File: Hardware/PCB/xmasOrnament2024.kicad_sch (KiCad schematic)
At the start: 54 parts, among them IC1 TP4056-42, Q1 AO3401A, Q2 CJ3400, SW1 BZCN_TSA007A1518B03, SW2 BZCN_TSA007A1518B03, U1 STM32C011F6

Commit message: Fixes.
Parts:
- added R14: 100k, Borna KiCAD Library:R0603, symbol Borna KiCAD Libary:R0603
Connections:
- net GND: now also R14.2
- net SW_CLK: now also R14.1
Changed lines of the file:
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@@
 	(wire
 		(pts
+			(xy 83.82 90.17) (xy 83.82 91.44)
+		)
+		(stroke
+			(width 0)
+			(type default)
+		)
+	)
+	(wire
+		(pts
 			(xy 59.69 88.9) (xy 59.69 90.17)
 		)
@@
 	(wire
 		(pts
+			(xy 85.09 90.17) (xy 83.82 90.17)
+		)
+		(stroke
+			(width 0)
+			(type default)
+		)
+	)
+	(wire
+		(pts
 			(xy 266.7 101.6) (xy 264.16 101.6)
 		)
@@
 	(wire
 		(pts
+			(xy 92.71 90.17) (xy 105.41 90.17)
+		)
+		(stroke
+			(width 0)
+			(type default)
+		)
+	)
+	(wire
+		(pts
 			(xy 72.39 38.1) (xy 64.77 38.1)
 		)
@@
 		)
 	)
+	(label "SW_CLK"
+		(at 105.41 90.17 180)
+		(fields_autoplaced yes)
+		(effects
+			(font
+				(size 1.27 1.27)
+			)
+			(justify right bottom)
+		)
+	)
 	(label "GND"
 		(at 121.92 100.33 180)
@@
 	)
 	(symbol
+		(lib_id "Borna KiCAD Libary:R0603")
+		(at 88.9 90.17 180)
+		(unit 1)
+		(exclude_from_sim no)
+		(in_bom yes)
+		(on_board yes)
+		(dnp no)
+		(property "Reference" "R14"
+			(at 86.868 88.392 0)
+			(effects
+				(font
+					(size 1.27 1.27)
+				)
+				(justify right)
+			)
+		)
+		(property "Value" "100k"
+			(at 86.868 91.948 0)
+			(effects
+				(font
+					(size 1.27 1.27)
+				)
+				(justify right)
+			)
+		)
+		(property "Footprint" "Borna KiCAD Library:R0603"
+			(at 88.9 86.36 0)
+			(effects
+				(font
+					(size 1.27 1.27)
+				)
+				(hide yes)
+			)
+		)
+		(property "Datasheet" ""
+			(at 88.9 90.17 0)
+			(effects
+				(font
+					(size 1.27 1.27)
+				)
+				(hide yes)
+			)
+		)
+		(property "Description" ""
+			(at 88.9 90.17 0)
+			(effects
+				(font
+					(size 1.27 1.27)
+				)
+				(hide yes)
+			)
+		)
+		(pin "2"
+		)
+		(pin "1"
+		)
+		(instances
+			(project "xmasOrnamentV2"
+				(path "/4b586804-9690-4d72-8d9c-0efbd06b06d2"
+					(reference "R14")
+					(unit 1)
+				)
+			)
+		)
+	)
+	(symbol
 		(lib_id "Borna KiCAD Libary:WS2812B-2020")
 		(at 148.59 100.33 0)
@@
 		(dnp no)
 		(property "Reference" "R10"
-			(at 233.68 34.036 0)
+			(at 233.172 30.988 0)
 			(effects
 				(font
@@
 					(unit 1)
 				)
+			)
+		)
+	)
+	(symbol
+		(lib_id "power:GND")
+		(at 83.82 91.44 0)
+		(unit 1)
+		(exclude_from_sim no)
+		(in_bom yes)
+		(on_board yes)
+		(dnp no)
+		(property "Reference" "#PWR053"
+			(at 83.82 97.79 0)
+			(effects
+				(font
+					(size 1.27 1.27)
+				)
+				(hide yes)
+			)
+		)
+		(property "Value" "GND"
+			(at 83.82 94.996 0)
+			(effects
+				(font
+					(size 1.27 1.27)
+				)
+			)
+		)
+		(property "Footprint" ""
+			(at 83.82 91.44 0)
+			(effects
+				(font
+					(size 1.27 1.27)
+				)
+				(hide yes)
+			)
+		)
+		(property "Datasheet" ""
+			(at 83.82 91.44 0)
+			(effects
+				(font
+					(size 1.27 1.27)
+				)
+				(hide yes)
+			)
+		)
+		(property "Description" "Power symbol creates a global label with name \"GND\" , ground"
+			(at 83.82 91.44 0)
+			(effects
+				(font
+					(size 1.27 1.27)
+				)
+				(hide yes)
+			)
+		)
+		(pin "1"
+		)
+		(instances
+			(project "xmasOrnamentV2"
+				(path "/4b586804-9690-4d72-8d9c-0efbd06b06d2"
+					(reference "#PWR053")
+					(unit 1)
+				)

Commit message: Board finished.
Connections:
- net BTN1: now also U1.9 (PA2); no longer U1.7 (PA0)
- net BTN2: now also U1.7 (PA0); no longer U1.9 (PA2)
- net VDD: now also C1.2, CONN1.+, IC1.5 (BAT)
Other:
- moved on the sheet: CONN1
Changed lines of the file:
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@@
 	)
 	(junction
+		(at 113.03 40.64)
+		(diameter 0)
+		(color 0 0 0 0)
+	)
+	(junction
 		(at 176.53 60.96)
 		(diameter 0)
@@
 	(wire
 		(pts
+			(xy 115.57 31.75) (xy 115.57 36.83)
+		)
+		(stroke
+			(width 0)
+			(type default)
+		)
+	)
+	(wire
+		(pts
 			(xy 227.33 121.92) (xy 226.06 121.92)
 		)
@@
 	(wire
 		(pts
+			(xy 113.03 36.83) (xy 113.03 40.64)
+		)
+		(stroke
+			(width 0)
+			(type default)
+		)
+	)
+	(wire
+		(pts
 			(xy 43.18 100.33) (xy 44.45 100.33)
 		)
@@
 	(wire
 		(pts
-			(xy 99.06 48.26) (xy 99.06 43.18)
+			(xy 113.03 48.26) (xy 113.03 43.18)
 		)
 		(stroke
@@
 	(wire
 		(pts
+			(xy 115.57 36.83) (xy 113.03 36.83)
+		)
+		(stroke
+			(width 0)
+			(type default)
+		)
+	)
+	(wire
+		(pts
 			(xy 242.57 121.92) (xy 246.38 121.92)
 		)
@@
 	(wire
 		(pts
+			(xy 113.03 40.64) (xy 114.3 40.64)
+		)
+		(stroke
+			(width 0)
+			(type default)
+		)
+	)
+	(wire
+		(pts
 			(xy 223.52 115.57) (xy 223.52 119.38)
 		)
@@
 	(wire
 		(pts
-			(xy 93.98 40.64) (xy 100.33 40.64)
+			(xy 93.98 40.64) (xy 113.03 40.64)
 		)
 		(stroke
@@
 	(wire
 		(pts
-			(xy 99.06 43.18) (xy 100.33 43.18)
+			(xy 113.03 43.18) (xy 114.3 43.18)
 		)
 		(stroke
@@
 		)
 	)
-	(label "BTN1"
+	(label "BTN2"
 		(at 45.72 115.57 0)
 		(fields_autoplaced yes)
@@
 		)
 	)
-	(label "BTN2"
+	(label "BTN1"
 		(at 45.72 120.65 0)
 		(fields_autoplaced yes)
@@
 	(symbol
 		(lib_id "Borna KiCAD Libary:S2B-PH-SM4-TB")
-		(at 102.87 41.91 0)
+		(at 116.84 41.91 0)
 		(unit 1)
 		(exclude_from_sim no)
@@
 		(on_board yes)
 		(dnp no)
-		(fields_autoplaced yes)
 		(property "Reference" "CONN1"
-			(at 107.95 40.6399 0)
+			(at 122.428 45.466 90)
 			(effects
 				(font
@@
 		)
 		(property "Value" "S2B-PH-SM4-TB"
-			(at 107.95 43.1799 0)
+			(at 124.714 50.546 90)
 			(effects
 				(font
@@
 		)
 		(property "Footprint" "Borna KiCAD Library:JST_S2B-PH-SM4-TB"
-			(at 102.87 41.91 0)
+			(at 116.84 41.91 0)
 			(effects
 				(font
@@
 		)
 		(property "Datasheet" ""
-			(at 102.87 41.91 0)
+			(at 116.84 41.91 0)
 			(effects
 				(font
@@
 		)
 		(property "Description" ""
-			(at 102.87 41.91 0)
+			(at 116.84 41.91 0)
 			(effects
 				(font
@@
 	)
 	(symbol
+		(lib_id "power:VDD")
+		(at 115.57 31.75 0)
+		(unit 1)
+		(exclude_from_sim no)
+		(in_bom yes)
+		(on_board yes)
+		(dnp no)
+		(property "Reference" "#PWR054"
+			(at 115.57 35.56 0)
+			(effects
+				(font
+					(size 1.27 1.27)
+				)
+				(hide yes)
+			)
+		)
+		(property "Value" "VDD"
+			(at 115.57 28.194 0)
+			(effects
+				(font
+					(size 1.27 1.27)
+				)
+			)
+		)
+		(property "Footprint" ""
+			(at 115.57 31.75 0)
+			(effects
+				(font
+					(size 1.27 1.27)
+				)
+				(hide yes)
+			)
+		)
+		(property "Datasheet" ""
+			(at 115.57 31.75 0)
+			(effects
+				(font
+					(size 1.27 1.27)
+				)
+				(hide yes)
+			)
+		)
+		(property "Description" "Power symbol creates a global label with name \"VDD\""
+			(at 115.57 31.75 0)
+			(effects
+				(font
+					(size 1.27 1.27)
+				)
+				(hide yes)
+			)
+		)
+		(pin "1"
+		)
+		(instances
+			(project "xmasOrnamentV2"
+				(path "/4b586804-9690-4d72-8d9c-0efbd06b06d2"
+					(reference "#PWR054")
+					(unit 1)
+				)
+			)
+		)
+	)
+	(symbol
 		(lib_id "Borna KiCAD Libary:TP-1_5mm")
 		(at 110.49 115.57 0)
@@
 	(symbol
 		(lib_id "power:GND")
-		(at 99.06 48.26 0)
+		(at 113.03 48.26 0)
 		(unit 1)
 		(exclude_from_sim no)
@@
 		(dnp no)
 		(property "Reference" "#PWR09"
-			(at 99.06 54.61 0)
+			(at 113.03 54.61 0)
 			(effects
 				(font
@@
 		)
 		(property "Value" "GND"
-			(at 99.06 51.816 0)
+			(at 113.03 51.816 0)
 			(effects
 				(font
@@
 		)
 		(property "Footprint" ""
-			(at 99.06 48.26 0)
+			(at 113.03 48.26 0)
 			(effects
 				(font
@@
 		)
 		(property "Datasheet" ""
-			(at 99.06 48.26 0)
+			(at 113.03 48.26 0)
 			(effects
 				(font
@@
 		)
 		(property "Description" "Power symbol creates a global label with name \"GND\" , ground"
-			(at 99.06 48.26 0)
+			(at 113.03 48.26 0)
 			(effects
 				(font

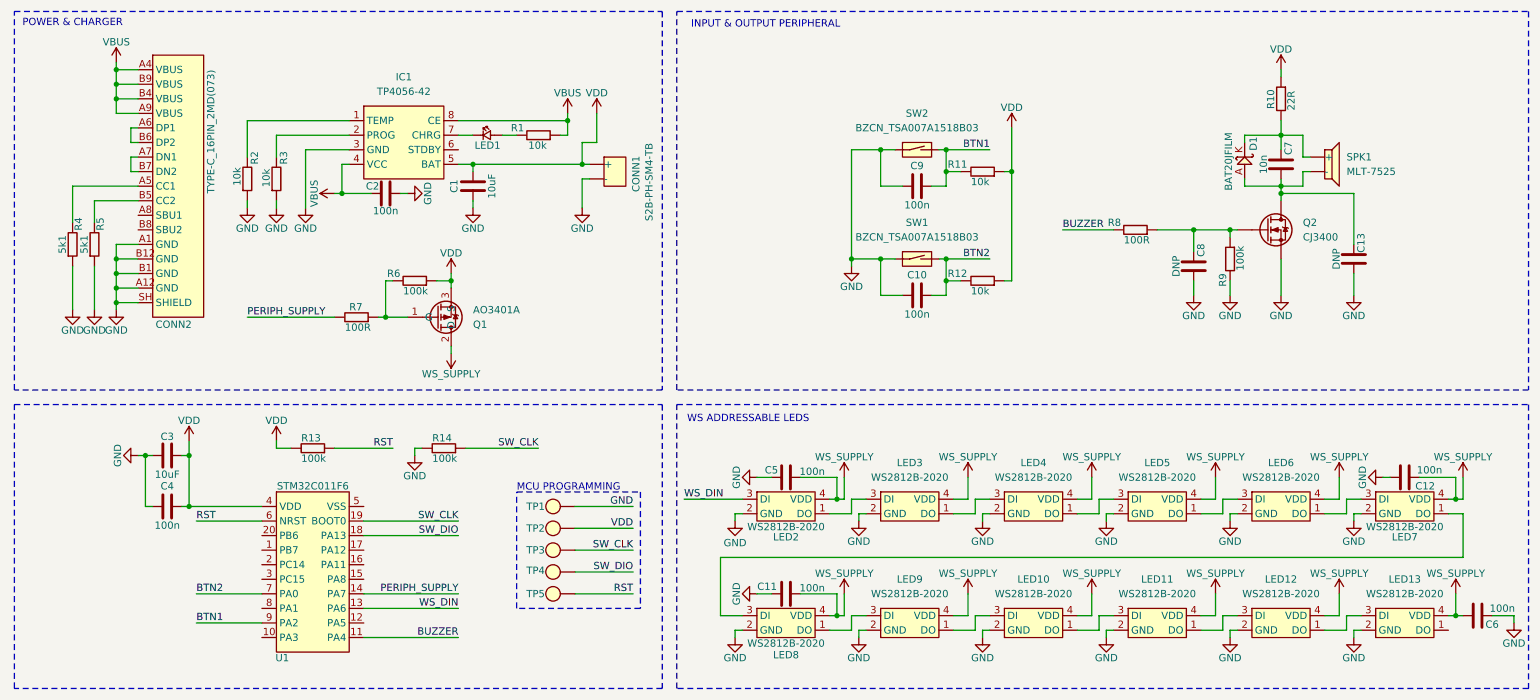
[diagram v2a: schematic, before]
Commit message: Added VREG.
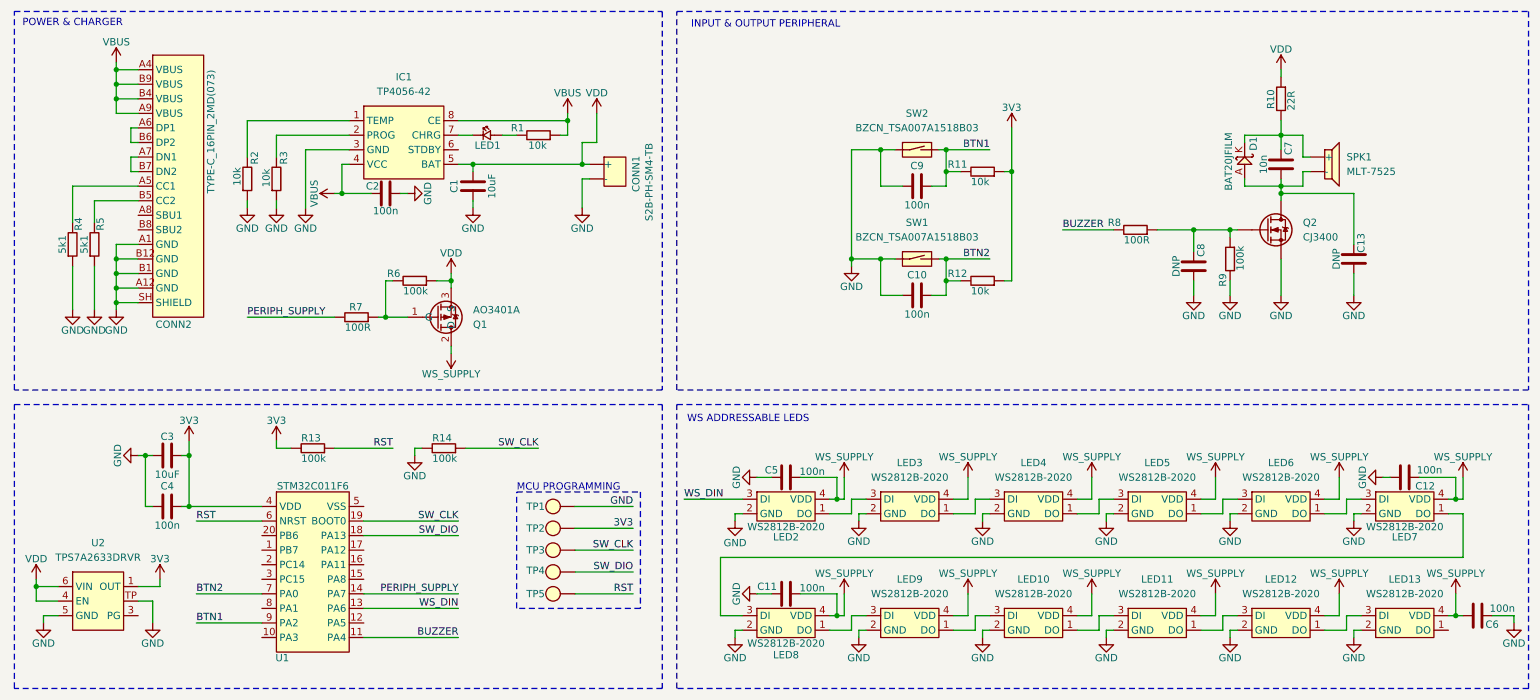
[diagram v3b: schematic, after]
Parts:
- added U2: TPS7A2633DRVR, Borna KiCAD Library:WSON-6, symbol Borna KiCAD Libary:TPS7A2633DRVR
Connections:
- net GND: now also U2.5 (GND), U2.TP
- net VDD: now also U2.4 (EN), U2.6 (VIN); no longer C3.2, C4.2, R11.1, R12.1, R13.2, TP2.1 (TP), U1.4 (VDD)
- new net 3V3: C3.2, C4.2, R11.1, R12.1, R13.2, TP2.1 (TP), U1.4 (VDD), U2.1 (OUT)
